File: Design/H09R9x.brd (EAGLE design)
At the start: 34.6 x 30 mm, 24 parts, among them P1 HEXABIT_17.32, U1 STM32F091CBU6, U2 TSD305-1C55, X1 XTALL_CSTCE8M00G52

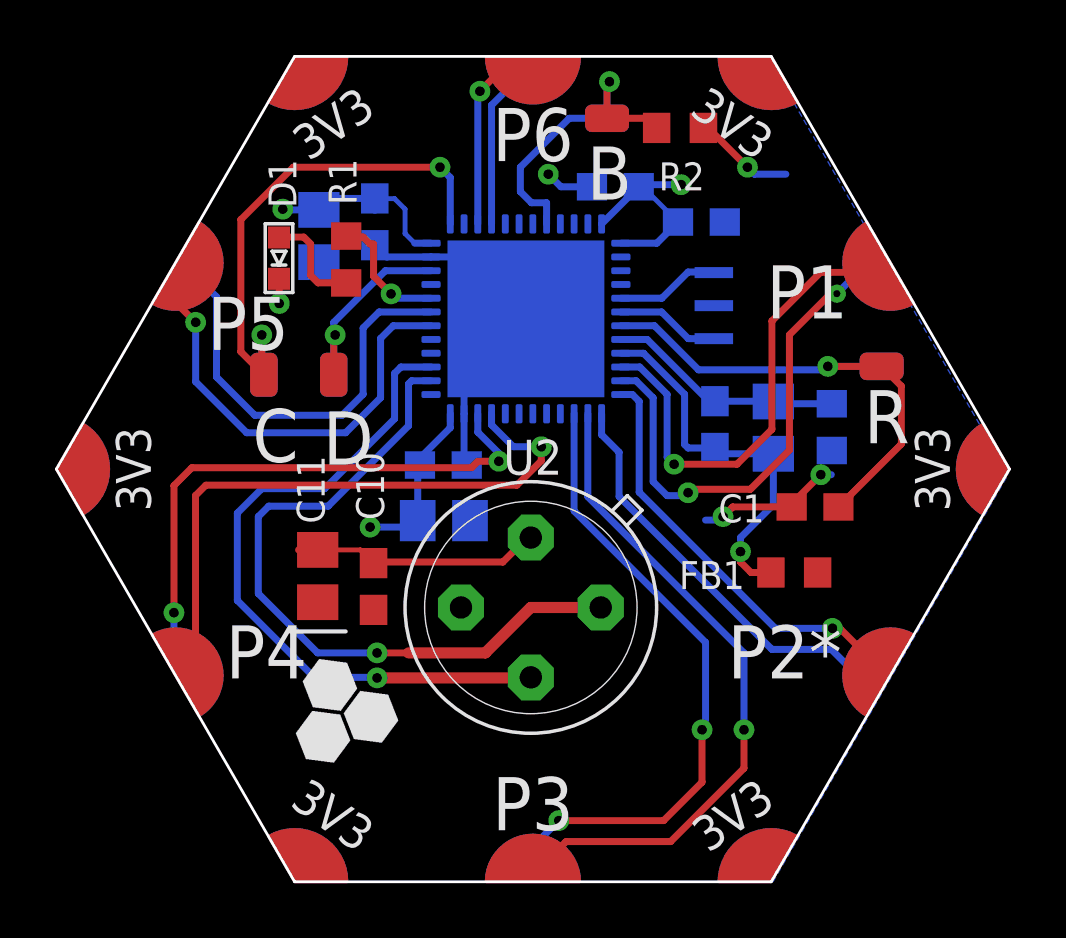
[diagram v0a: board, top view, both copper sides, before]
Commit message: chage thermopile print to last version
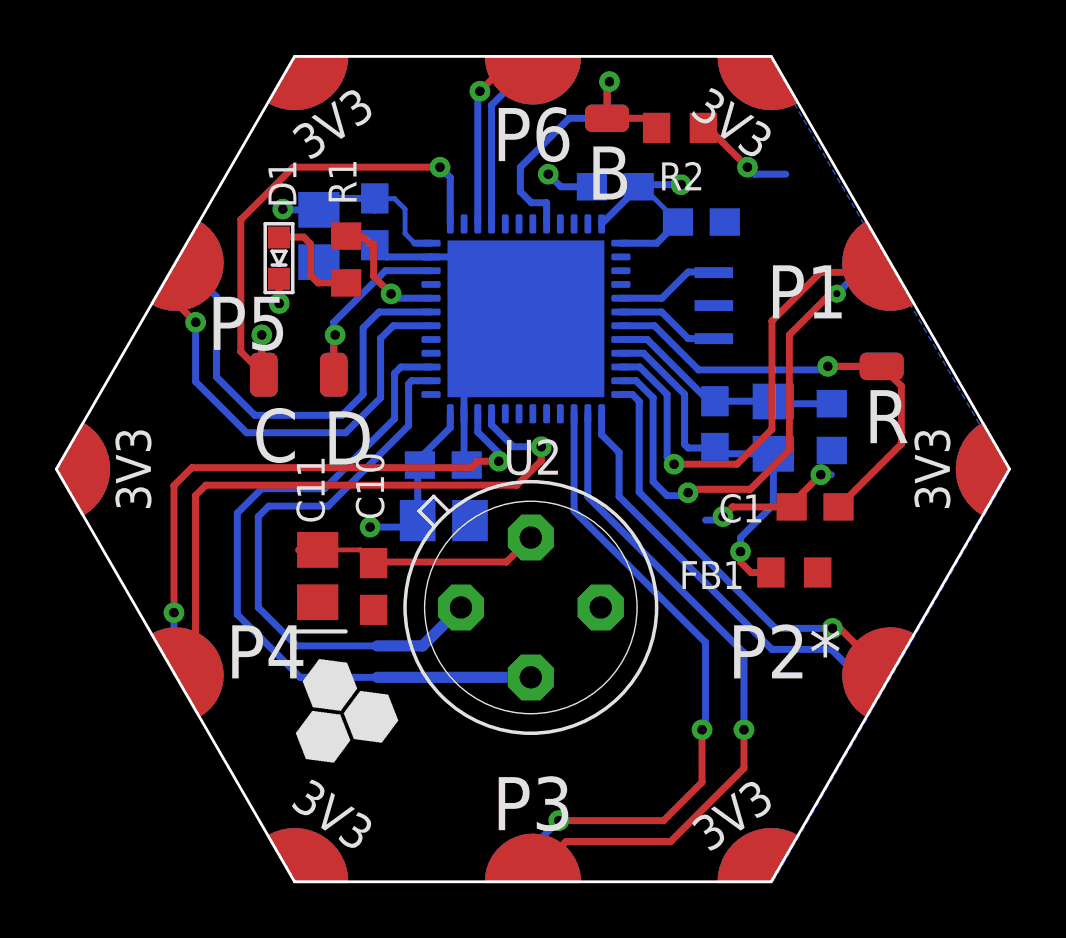
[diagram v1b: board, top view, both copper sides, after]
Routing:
- net I2C2_SCL: track 26.0 -> 21.0 mm, vias 1 -> 0
- net I2C2_SDA: track 25.2 -> 25.5 mm, vias 1 -> 0
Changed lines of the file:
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@@
 </element>
 <element name="P1" library="Hexabitz" package="HEXABIT_17.32" value="HEXABIT_17.32" x="34.6202" y="34.6202" smashed="yes"/>
-<element name="U2" library="HEXABITZ_ICs" library_urn="urn:adsk.eagle:library:20064554" package="TEMPERATURESENSOR-TO5" package3d_urn="urn:adsk.eagle:package:22912731/1" value="TSD305-1C55" x="34.544" y="29.591" smashed="yes" rot="R180">
+<element name="U2" library="HEXABITZ_ICs" library_urn="urn:adsk.eagle:library:20064554" package="TEMPERATURESENSOR-TO5" package3d_urn="urn:adsk.eagle:package:22912731/2" value="TSD305-1C55" x="34.544" y="29.591" smashed="yes" rot="R180">
 <attribute name="MFN" value="TE Connectivity" x="34.544" y="29.591" size="1.778" layer="27" rot="R180" display="off"/>
 <attribute name="MPN" value="G-TPMO-101" x="34.544" y="29.591" size="1.778" layer="27" rot="R180" display="off"/>
@@
 <contactref element="U1" pad="P$47"/>
 <contactref element="U1" pad="EP"/>
-<wire x1="34.544" y1="32.131" x2="34.417" y2="32.131" width="0.254" layer="1"/>
-<wire x1="34.417" y1="32.131" x2="33.528" y2="31.242" width="0.254" layer="1"/>
-<wire x1="29.122" y1="31.242" x2="33.528" y2="31.242" width="0.254" layer="1"/>
+<wire x1="34.544" y1="32.131" x2="33.655" y2="31.242" width="0.254" layer="1"/>
+<wire x1="29.122" y1="31.242" x2="33.655" y2="31.242" width="0.254" layer="1"/>
 <wire x1="26.797" y1="31.684" x2="26.736" y2="31.623" width="0.254" layer="1"/>
 <wire x1="25.391109375" y1="41.537946875" x2="25.4" y2="41.52905625" width="0.254" layer="1"/>
@@
 <contactref element="U1" pad="P$36"/>
 <contactref element="U1" pad="P$48"/>
-<wire x1="32.004" y1="29.591" x2="31.789" y2="29.376" width="0.254" layer="1"/>
 <wire x1="27.078" y1="29.503" x2="26.797" y2="29.784" width="0.254" layer="1"/>
 <wire x1="26.841696875" y1="44.042146875" x2="25.553853125" y2="44.042146875" width="0.254" layer="16"/>
@@
 <wire x1="37.1162" y1="36.63119375" x2="37.1162" y2="35.86919375" width="0.254" layer="16"/>
 <wire x1="37.7512" y1="35.23419375" x2="37.7512" y2="33.6228" width="0.254" layer="16"/>
-<wire x1="47.1372" y1="27.4522" x2="47.0282" y2="27.4522" width="0.254" layer="16"/>
 <wire x1="47.0102" y1="27.4702" x2="47.0282" y2="27.4522" width="0.254" layer="16"/>
 <wire x1="43.307" y1="28.067" x2="45.466" y2="28.067" width="0.254" layer="16"/>
@@
 <wire x1="27.178" y1="33.274" x2="25.019" y2="33.274" width="0.254" layer="16"/>
 <wire x1="25.019" y1="33.274" x2="24.638" y2="32.893" width="0.254" layer="16"/>
-<wire x1="24.638" y1="32.893" x2="24.638" y2="30.099" width="0.254" layer="16"/>
-<wire x1="24.638" y1="30.099" x2="26.797" y2="27.94" width="0.254" layer="16"/>
-<wire x1="26.797" y1="27.94" x2="28.956" y2="27.94" width="0.254" layer="16"/>
-<via x="28.956" y="27.94" extent="1-16" drill="0.35"/>
-<wire x1="28.956" y1="27.94" x2="30.099" y2="27.94" width="0.254" layer="1"/>
-<wire x1="30.099" y1="27.94" x2="32.893" y2="27.94" width="0.4064" layer="1"/>
-<wire x1="32.893" y1="27.94" x2="34.544" y2="29.591" width="0.4064" layer="1"/>
-<wire x1="34.544" y1="29.591" x2="37.084" y2="29.591" width="0.4064" layer="1"/>
+<wire x1="24.638" y1="32.893" x2="24.638" y2="29.591" width="0.254" layer="16"/>
+<wire x1="24.638" y1="29.591" x2="26.035" y2="28.194" width="0.254" layer="16"/>
+<wire x1="28.956" y1="28.194" x2="26.035" y2="28.194" width="0.254" layer="16"/>
+<wire x1="28.956" y1="28.194" x2="30.607" y2="28.194" width="0.4064" layer="16"/>
+<wire x1="30.607" y1="28.194" x2="32.004" y2="29.591" width="0.4064" layer="16"/>
 </signal>
 <signal name="I2C2_SDA">
@@
 <wire x1="29.591" y1="38.1" x2="29.591" y2="36.449" width="0.254" layer="16"/>
 <wire x1="27.051" y1="33.909" x2="24.765" y2="33.909" width="0.254" layer="16"/>
-<wire x1="23.876" y1="33.02" x2="23.876" y2="29.845" width="0.254" layer="16"/>
+<wire x1="23.876" y1="33.02" x2="23.876" y2="29.337" width="0.254" layer="16"/>
 <wire x1="29.591" y1="36.449" x2="27.051" y2="33.909" width="0.254" layer="16"/>
 <wire x1="24.765" y1="33.909" x2="23.876" y2="33.02" width="0.254" layer="16"/>
-<wire x1="26.67" y1="27.051" x2="28.956" y2="27.051" width="0.254" layer="16"/>
-<wire x1="23.876" y1="29.845" x2="26.67" y2="27.051" width="0.254" layer="16"/>
-<wire x1="28.956" y1="27.051" x2="28.956" y2="27.0312" width="0.4064" layer="16"/>
-<via x="28.956" y="27.0312" extent="1-16" drill="0.35"/>
-<wire x1="28.956" y1="27.0312" x2="34.5242" y2="27.0312" width="0.4064" layer="1"/>
-<wire x1="34.5242" y1="27.0312" x2="34.544" y2="27.051" width="0.4064" layer="1"/>
+<wire x1="26.162" y1="27.051" x2="28.956" y2="27.051" width="0.254" layer="16"/>
+<wire x1="23.876" y1="29.337" x2="26.162" y2="27.051" width="0.254" layer="16"/>
+<wire x1="28.956" y1="27.051" x2="34.544" y2="27.051" width="0.4064" layer="16"/>
 </signal>
 <signal name="IMU_INT2">
